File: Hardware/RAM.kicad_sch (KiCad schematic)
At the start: 2 parts, among them U7 S80KS5123GABHA020, U8 S80KS5123GABHA020

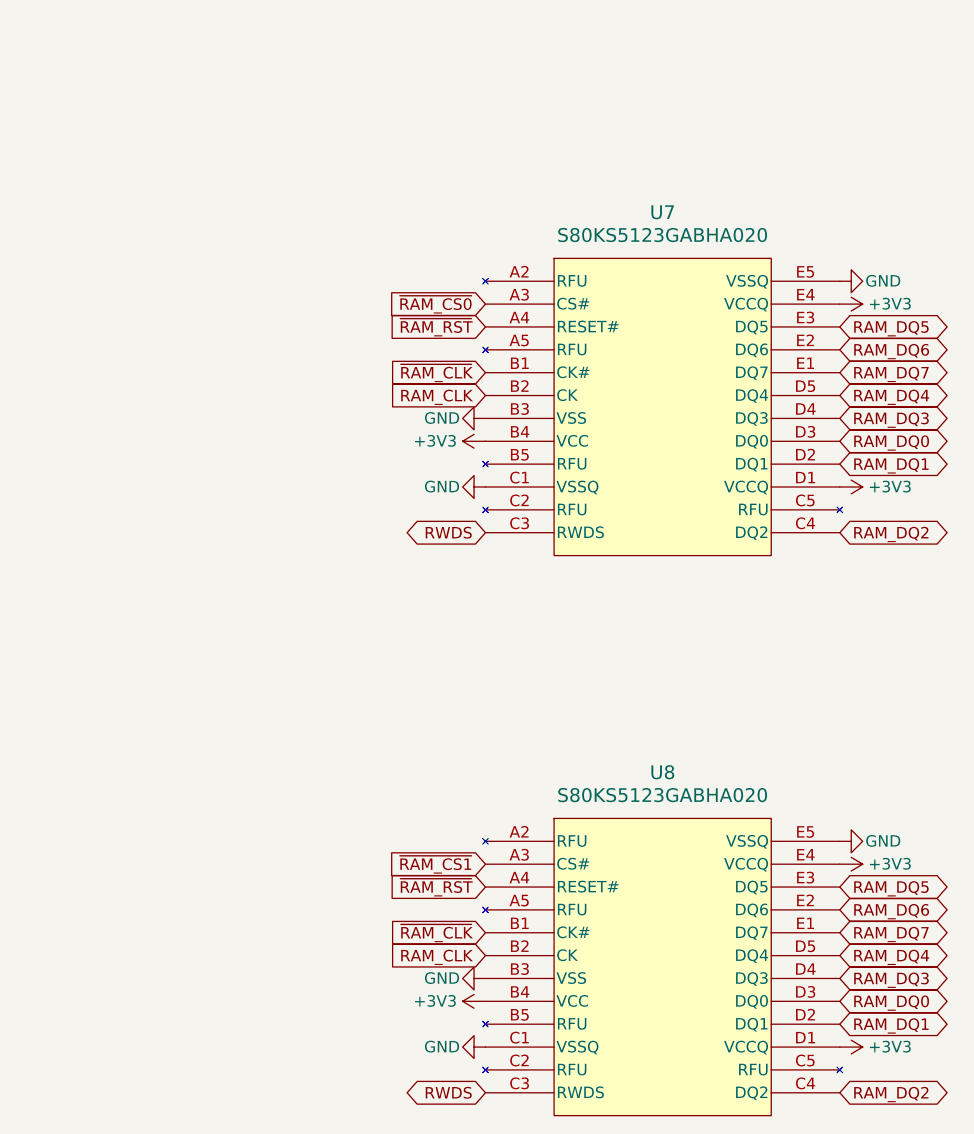
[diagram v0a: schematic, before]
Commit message: 11/21 update
finished annotating the schematic and add pictures and output the pdf
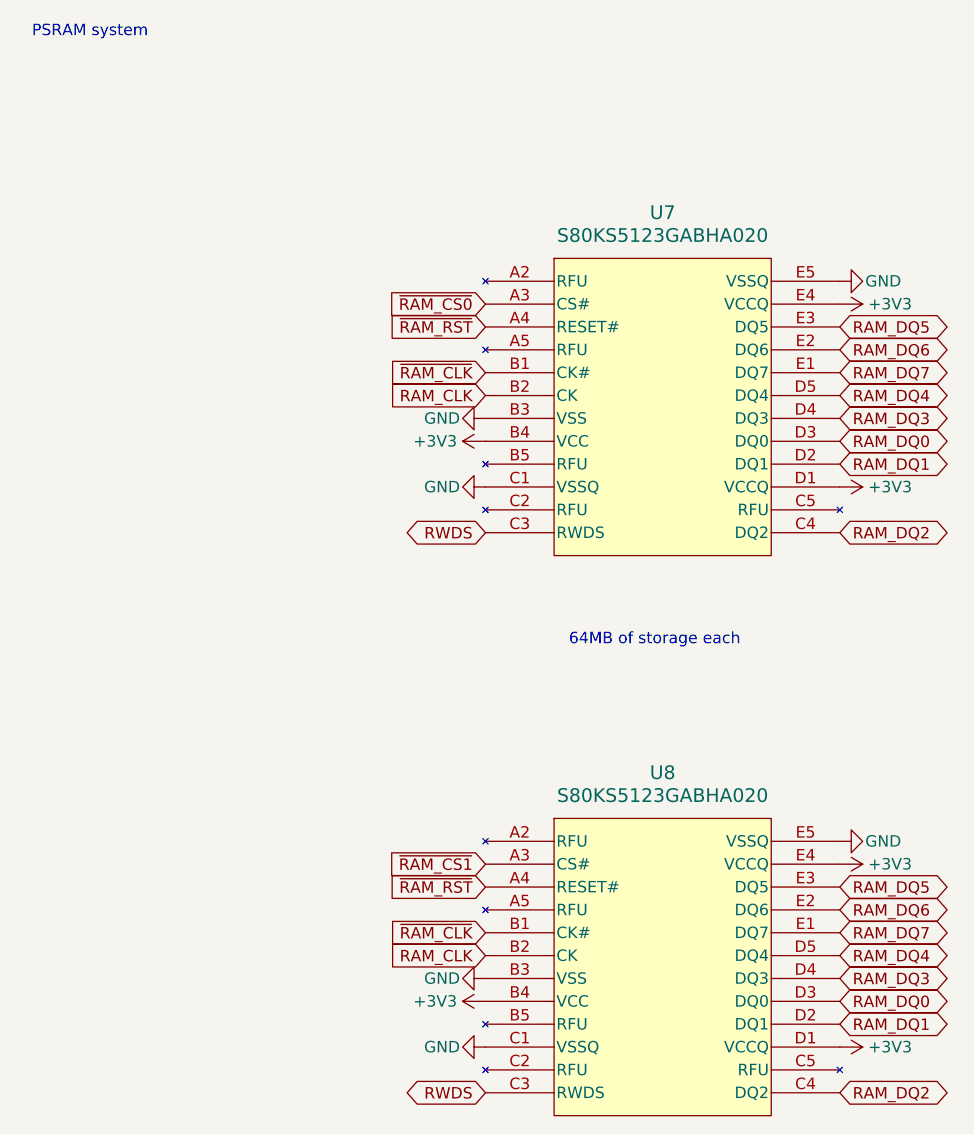
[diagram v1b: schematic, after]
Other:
- note added: "64MB of storage each"
- note added: "PSRAM system"
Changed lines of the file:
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@@
 	(generator_version "8.0")
 	(paper "A4")
+	(text "64MB of storage each"
+		(exclude_from_sim no)
+		(at 86.106 84.328 0)
+		(effects
+			(font
+				(size 1.27 1.27)
+			)
+		)
+	)
+	(text "PSRAM system"
+		(exclude_from_sim no)
+		(at 23.368 16.764 0)
+		(effects
+			(font
+				(size 1.27 1.27)
+			)
+		)
+	)
 	(global_label "~{RAM_CLK}"
 		(shape input)
